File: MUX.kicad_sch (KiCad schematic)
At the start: 22 parts, among them Q1 RK7002T116, Q2 RK7002T116, Q3 RK7002T116, Q4 RK7002T116, U3 MC74AC138DR2G, U4 MC74AC138DR2G

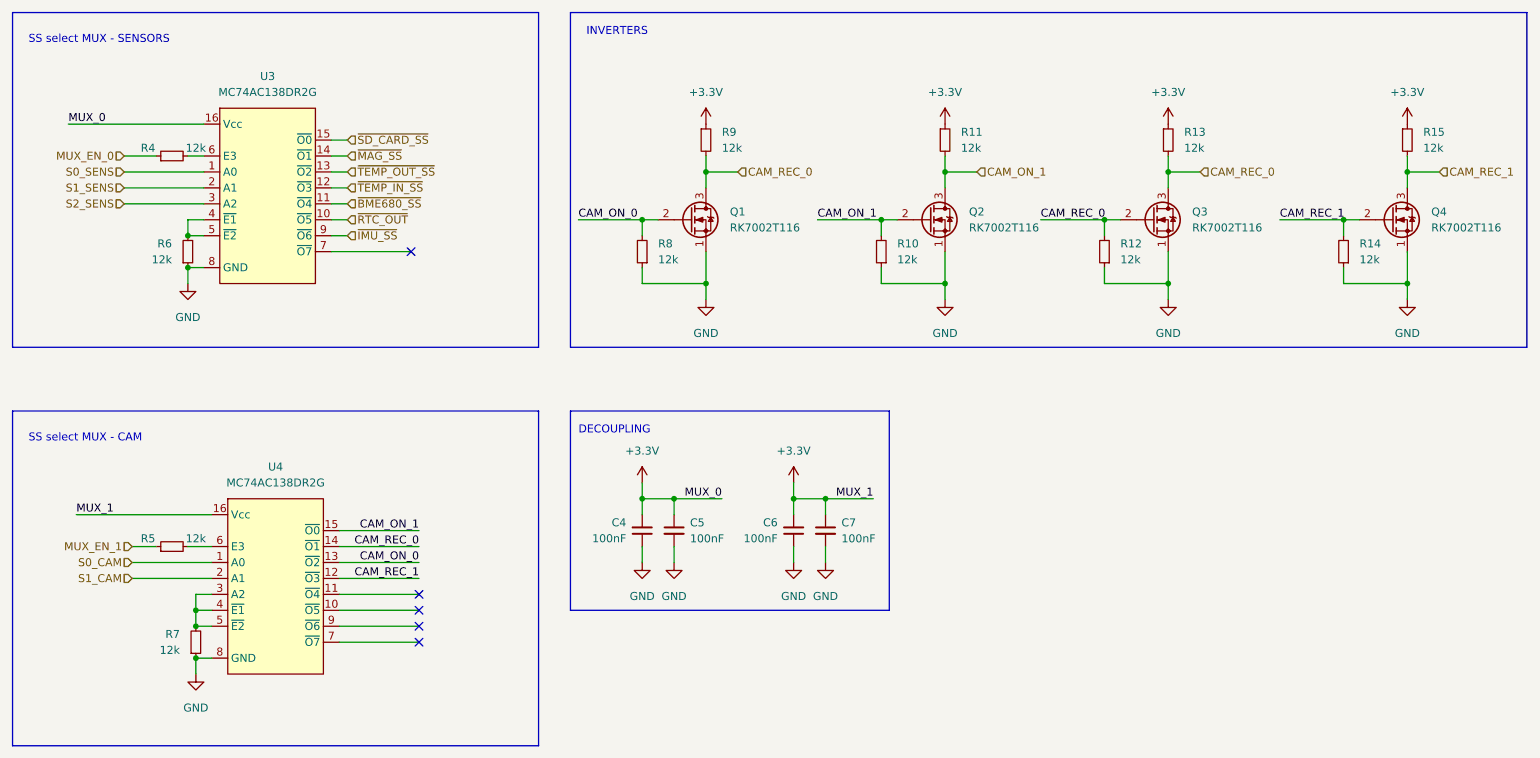
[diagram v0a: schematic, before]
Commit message: 0.3v KiCad
Needs improvements:
-Visual
-Better grounding
-Component placement
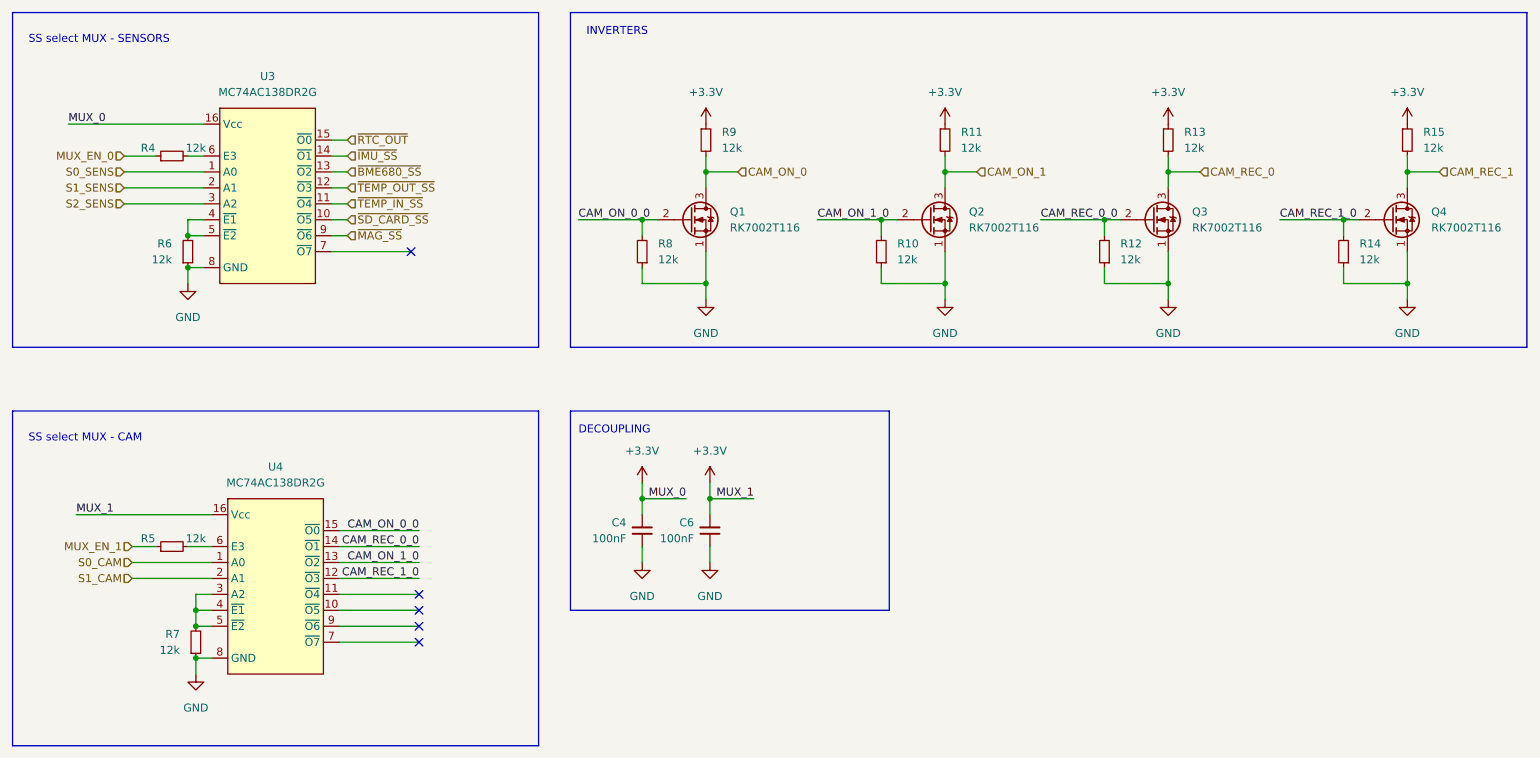
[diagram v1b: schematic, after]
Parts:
- removed C5, C7: 100nF, Capacitor_SMD:C_0402_1005Metric, symbol Device:C_Small
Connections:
- net CAM_ON_0: now also Q1.3 (D), R9.2; no longer Q1.2 (G), R8.2, U4.13 (~{O2})
- net CAM_ON_1: no longer Q2.2 (G), R10.2, U4.15 (~{O0})
- net CAM_REC_0: no longer Q1.3 (D), Q3.2 (G), R12.2, R9.2, U4.14 (~{O1})
- net CAM_REC_1: no longer Q4.2 (G), R14.2, U4.12 (~{O3})
- net ~{BME680_SS}: now also U3.13 (~{O2}); no longer U3.11 (~{O4})
- net ~{IMU_SS}: now also U3.14 (~{O1}); no longer U3.9 (~{O6})
- net ~{MAG_SS}: now also U3.9 (~{O6}); no longer U3.14 (~{O1})
- net ~{RTC_OUT}: now also U3.15 (~{O0}); no longer U3.10 (~{O5})
- net ~{SD_CARD_SS}: now also U3.10 (~{O5}); no longer U3.15 (~{O0})
- net ~{TEMP_IN_SS}: now also U3.11 (~{O4}); no longer U3.12 (~{O3})
- net ~{TEMP_OUT_SS}: now also U3.12 (~{O3}); no longer U3.13 (~{O2})
- new net CAM_ON_0_0: Q1.2 (G), R8.2, U4.15 (~{O0})
- new net CAM_ON_1_0: Q2.2 (G), R10.2, U4.13 (~{O2})
- new net CAM_REC_0_0: Q3.2 (G), R12.2, U4.14 (~{O1})
- new net CAM_REC_1_0: Q4.2 (G), R14.2, U4.12 (~{O3})
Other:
- moved on the sheet: C6

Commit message: V1
- Corrected SD-cards footprint and schematical represantation;
- Corrected RTC shematics:
	- changed oscilators power supply from internal 3v3 to Vbat so RTC works when PCB is disconnected from external power supply [PWR PCB];
	- 32 kHz to microcontroller now comes from RTC module;
	- added 100 nF decoupling capacitor to Vbat RTC pin.
- Corrected couple connections and component placement on PCB
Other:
- company: (none) -> BASEMENT
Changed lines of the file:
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@@
 (kicad_sch (version 20211123) (generator eeschema)
   (paper "A4")
+  (title_block
+    (date "%%date%%")
+    (rev "%%version%%")
+    (company "BASEMENT")
+  )
   (junction (at 237.49 60.96) (diameter 0) (color 0 0 0 0)
   )
@@
     (stroke (width 0) (type default) (color 0 0 0 0))
   )
+  (wire (pts (xy 25.4 97.79) (xy 46.99 97.79))
+    (stroke (width 0) (type default) (color 0 0 0 0))
+  )
   (wire (pts (xy 163.83 43.18) (xy 163.83 45.72))
     (stroke (width 0) (type default) (color 0 0 0 0))
@@
   )
   (wire (pts (xy 227.33 60.96) (xy 237.49 60.96))
-    (stroke (width 0) (type default) (color 0 0 0 0))
-  )
-  (wire (pts (xy 25.4 97.79) (xy 46.99 97.79))
     (stroke (width 0) (type default) (color 0 0 0 0))
   )
@@
     (pin "1")
   )
-  (symbol (lib_name "MC74AC138DR2G_1") (lib_id "schematics:MC74AC138DR2G") (at 55.88 45.72 0) (unit 1)
+  (symbol (lib_id "Device:R_Small") (at 43.18 55.88 0) (mirror x) (unit 1)
+    (in_bom yes) (on_board yes) (fields_autoplaced)
+    (property "Reference" "R6" (id 0) (at 40.64 54.6099 0)
+      (effects (font (size 1.27 1.27)) (justify right))
+    )
+    (property "Value" "12k" (id 1) (at 40.64 57.1499 0)
+      (effects (font (size 1.27 1.27)) (justify right))
+    )
+    (property "Footprint" "Resistor_SMD:R_0402_1005Metric" (id 2) (at 43.18 55.88 0)
+      (effects (font (size 1.27 1.27)) hide)
+    )
+    (property "Datasheet" "~" (id 3) (at 43.18 55.88 0)
+      (effects (font (size 1.27 1.27)) hide)
+    )
+    (pin "1")
+    (pin "2")
+  )
+  (symbol (lib_id "schematics:MC74AC138DR2G") (at 55.88 45.72 0) (unit 1)
     (in_bom yes) (on_board yes) (fields_autoplaced)
     (property "Reference" "U3" (id 0) (at 55.88 27.94 0))
@@
     (pin "9")
   )
-  (symbol (lib_id "Device:R_Small") (at 43.18 55.88 0) (mirror x) (unit 1)
-    (in_bom yes) (on_board yes) (fields_autoplaced)
-    (property "Reference" "R6" (id 0) (at 40.64 54.6099 0)
-      (effects (font (size 1.27 1.27)) (justify right))
-    )
-    (property "Value" "12k" (id 1) (at 40.64 57.1499 0)
-      (effects (font (size 1.27 1.27)) (justify right))
-    )
-    (property "Footprint" "Resistor_SMD:R_0402_1005Metric" (id 2) (at 43.18 55.88 0)
-      (effects (font (size 1.27 1.27)) hide)
-    )
-    (property "Datasheet" "~" (id 3) (at 43.18 55.88 0)
-      (effects (font (size 1.27 1.27)) hide)
-    )
-    (pin "1")
-    (pin "2")
-  )
   (symbol (lib_id "power:+3.3V") (at 125.73 35.56 0) (unit 1)
     (in_bom yes) (on_board yes)
@@
     (pin "2")
   )
-  (symbol (lib_name "MC74AC138DR2G_1") (lib_id "schematics:MC74AC138DR2G") (at 57.15 107.95 0) (unit 1)
+  (symbol (lib_id "schematics:MC74AC138DR2G") (at 57.15 107.95 0) (unit 1)
     (in_bom yes) (on_board yes) (fields_autoplaced)
     (property "Reference" "U4" (id 0) (at 57.15 90.17 0))
